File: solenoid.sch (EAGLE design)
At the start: 43 parts, among them U1 QS5K2TR, U2 QS5K2TR, U3 QS5K2TR, U4 QS5K2TR, U5 QS5K2TR, U6 QS5K2TR, Y1 ECS-80-S-4X

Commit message: potentially finished schematic
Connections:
- new net SOLI1_1: U1.TR1_DRAIN
- new net SOLI1_2: U1.TR2_DRAIN
- net GPIO0: now also U2.TR2_GATE
- net GPIO1: now also U2.TR1_GATE
- net GPIO10: now also U4.TR1_GATE
- net GPIO11: now also U4.TR2_GATE
- net GPIO12: now also U5.TR1_GATE
- net GPIO13: now also U5.TR2_GATE
- net GPIO14: now also U6.TR1_GATE
- net GPIO15: now also U6.TR2_GATE
- net GPIO2: now also U1.TR2_GATE
- net GPIO3: now also U1.TR1_GATE
- net GPIO8: now also U3.TR1_GATE
- net GPIO9: now also U3.TR2_GATE
- net SOL2_1: now also U2.TR1_DRAIN
- net SOL2_2: now also U2.TR2_DRAIN
- net SOL3_1: now also U3.TR1_DRAIN
- net SOL3_2: now also U3.TR2_DRAIN
- net SOL4_1: now also U4.TR1_DRAIN
- net SOL4_2: now also U4.TR2_DRAIN
- net SOL5_1: now also U5.TR1_DRAIN
- net SOL5_2: now also U5.TR2_DRAIN
- net SOL6_1: now also U6.TR1_DRAIN
- net SOL6_2: now also U6.TR2_DRAIN
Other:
- note added: "NMOS ARRAY"
- moved on the sheet: U1, U2, U3, U4, U5, U6

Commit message: solenoid work
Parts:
- removed U3, U4, U5, U6: QS5K2TR, QS5K2TR:QS5K2TR
- U1, U2: value QS5K2TR -> ULN2003V12; device QS5K2TR:QS5K2TR -> ULN2003V12:ULN2003V12
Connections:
- removed net SOLI1_1: U1.TR1_DRAIN
- removed net SOLI1_2: U1.TR2_DRAIN
- net 12V: now also U1.COM, U2.COM; no longer U1.TR1_TR2_SOURCE, U2.TR1_TR2_SOURCE, U3.TR1_TR2_SOURCE, U4.TR1_TR2_SOURCE, U5.TR1_TR2_SOURCE, U6.TR1_TR2_SOURCE
- net GND: now also U1.GND, U2.GND
- net GPIO0: now also U1.IN6; no longer U2.TR2_GATE
- net GPIO1: now also U1.IN5; no longer U2.TR1_GATE
- net GPIO10: now also U2.IN3; no longer U4.TR1_GATE
- net GPIO11: now also U2.IN4; no longer U4.TR2_GATE
- net GPIO12: now also U2.IN5; no longer U5.TR1_GATE
- net GPIO13: now also U2.IN6; no longer U5.TR2_GATE
- net GPIO14: now also U1.IN1; no longer U6.TR1_GATE
- net GPIO15: now also U1.IN2; no longer U6.TR2_GATE
- net GPIO2: now also U1.IN4; no longer U1.TR2_GATE
- net GPIO3: now also U1.IN3; no longer U1.TR1_GATE
- net GPIO8: now also U2.IN1; no longer U3.TR1_GATE
- net GPIO9: now also U2.IN2; no longer U3.TR2_GATE
- net SOL1_1: now also U1.OUT3
- net SOL1_2: now also U1.OUT4
- net SOL2_1: now also U1.OUT5; no longer U2.TR1_DRAIN
- net SOL2_2: now also U1.OUT6; no longer U2.TR2_DRAIN
- net SOL3_1: now also U2.OUT1; no longer U3.TR1_DRAIN
- net SOL3_2: now also U2.OUT2; no longer U3.TR2_DRAIN
- net SOL4_1: now also U2.OUT3; no longer U4.TR1_DRAIN
- net SOL4_2: now also U2.OUT4; no longer U4.TR2_DRAIN
- net SOL5_1: now also U2.OUT5; no longer U5.TR1_DRAIN
- net SOL5_2: now also U2.OUT6; no longer U5.TR2_DRAIN
- net SOL6_1: now also U1.OUT1; no longer U6.TR1_DRAIN
- net SOL6_2: now also U1.OUT2; no longer U6.TR2_DRAIN

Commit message: uwu
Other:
- note added: "NPN Array"
- note removed: "NMOS ARRAY"
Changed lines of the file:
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@@
 <text x="342.9" y="55.88" size="1.778" layer="91">Pin 5 (VDDA)</text>
 <text x="370.84" y="-33.02" size="5.08" layer="91">T21 Connector for 12V, CAN, GND</text>
-<text x="10.16" y="-17.78" size="6.4516" layer="91">NMOS ARRAY</text>
+<text x="10.16" y="-17.78" size="6.4516" layer="91">NPN Array</text>
 </plain>
 <instances>

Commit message: k
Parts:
- removed U2: ULN2003V12, ULN2003V12:ULN2003V12
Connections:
- removed net SOL1_2: J1.1, U1.OUT4
- removed net SOL2_2: J2.1, U1.OUT6
- removed net SOL3_2: J5.1, U2.OUT2
- removed net SOL4_2: J6.1, U2.OUT4
- removed net SOL5_2: J7.1, U2.OUT6
- removed net SOL6_2: J8.1, U1.OUT2
- new net GPIO4: U1.IN4
- new net GPIO5: U1.IN5
- new net GPIO6: U1.IN6
- net 12V: now also J1.1, J2.1, J5.1, J6.1, J7.1, J8.1; no longer U2.COM
- net GND: no longer U2.GND
- net GPIO0: no longer U1.IN6
- net GPIO1: now also U1.IN1; no longer U1.IN5
- net GPIO10: no longer U2.IN3
- net GPIO11: no longer U2.IN4
- net GPIO12: no longer U2.IN5
- net GPIO13: no longer U2.IN6
- net GPIO14: no longer U1.IN1
- net GPIO15: no longer U1.IN2
- net GPIO2: now also U1.IN2; no longer U1.IN4
- net GPIO8: no longer U2.IN1
- net GPIO9: no longer U2.IN2
- net SOL1_1: now also U1.OUT1; no longer U1.OUT3
- net SOL2_1: now also U1.OUT2; no longer U1.OUT5
- net SOL3_1: now also U1.OUT3; no longer U2.OUT1
- net SOL4_1: now also U1.OUT4; no longer U2.OUT3
- net SOL5_1: now also U1.OUT5; no longer U2.OUT5
- net SOL6_1: now also U1.OUT6; no longer U1.OUT1

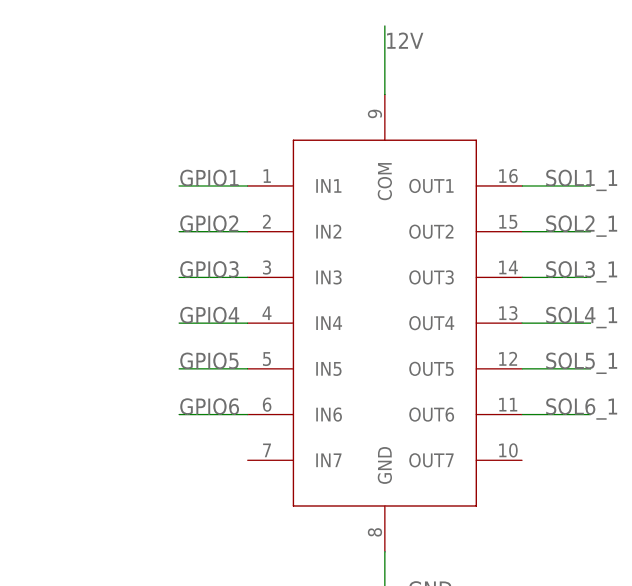
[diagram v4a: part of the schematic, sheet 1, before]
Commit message: next I make solenoid thingies 20 width
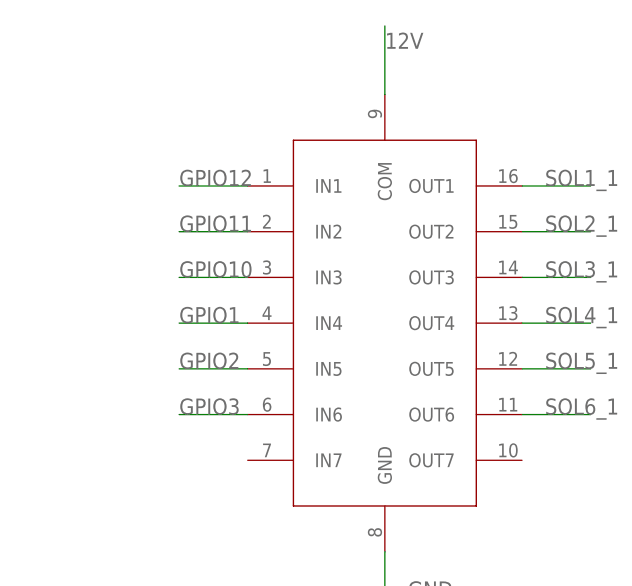
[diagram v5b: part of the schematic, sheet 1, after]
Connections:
- removed net GPIO4: U1.IN4
- removed net GPIO5: U1.IN5
- removed net GPIO6: U1.IN6
- net GPIO1: now also U1.IN4; no longer U1.IN1
- net GPIO10: now also U1.IN3
- net GPIO11: now also U1.IN2
- net GPIO12: now also U1.IN1
- net GPIO2: now also U1.IN5; no longer U1.IN2
- net GPIO3: now also U1.IN6; no longer U1.IN3
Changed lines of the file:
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@@
 </segment>
 <segment>
-<wire x1="15.24" y1="-50.8" x2="7.62" y2="-50.8" width="0.1524" layer="91"/>
-<label x="7.62" y="-50.8" size="1.778" layer="95"/>
-<pinref part="U1" gate="G$1" pin="IN1"/>
+<wire x1="15.24" y1="-66.04" x2="7.62" y2="-66.04" width="0.1524" layer="91"/>
+<label x="7.62" y="-66.04" size="1.778" layer="95"/>
+<pinref part="U1" gate="G$1" pin="IN4"/>
 </segment>
 </net>
@@
 </segment>
 <segment>
-<wire x1="15.24" y1="-60.96" x2="7.62" y2="-60.96" width="0.1524" layer="91"/>
-<label x="7.62" y="-60.96" size="1.778" layer="95"/>
-<pinref part="U1" gate="G$1" pin="IN3"/>
+<wire x1="15.24" y1="-76.2" x2="7.62" y2="-76.2" width="0.1524" layer="91"/>
+<label x="7.62" y="-76.2" size="1.778" layer="95"/>
+<pinref part="U1" gate="G$1" pin="IN6"/>
 </segment>
 </net>
@@
 </segment>
 <segment>
-<wire x1="15.24" y1="-55.88" x2="7.62" y2="-55.88" width="0.1524" layer="91"/>
-<label x="7.62" y="-55.88" size="1.778" layer="95"/>
-<pinref part="U1" gate="G$1" pin="IN2"/>
+<wire x1="15.24" y1="-71.12" x2="7.62" y2="-71.12" width="0.1524" layer="91"/>
+<label x="7.62" y="-71.12" size="1.778" layer="95"/>
+<pinref part="U1" gate="G$1" pin="IN5"/>
 </segment>
 </net>
@@
 <label x="350.52" y="99.06" size="1.778" layer="95" rot="R90"/>
 </segment>
+<segment>
+<wire x1="15.24" y1="-60.96" x2="7.62" y2="-60.96" width="0.1524" layer="91"/>
+<label x="7.62" y="-60.96" size="1.778" layer="95"/>
+<pinref part="U1" gate="G$1" pin="IN3"/>
+</segment>
 </net>
 <net name="GPIO9" class="0">
@@
 <label x="353.06" y="99.06" size="1.778" layer="95" rot="R90"/>
 </segment>
+<segment>
+<wire x1="15.24" y1="-55.88" x2="7.62" y2="-55.88" width="0.1524" layer="91"/>
+<label x="7.62" y="-55.88" size="1.778" layer="95"/>
+<pinref part="U1" gate="G$1" pin="IN2"/>
+</segment>
 </net>
 <net name="GPIO12" class="0">
@@
 <label x="358.14" y="99.06" size="1.778" layer="95" rot="R90"/>
 </segment>
+<segment>
+<wire x1="15.24" y1="-50.8" x2="7.62" y2="-50.8" width="0.1524" layer="91"/>
+<label x="7.62" y="-50.8" size="1.778" layer="95"/>
+<pinref part="U1" gate="G$1" pin="IN1"/>
+</segment>
 </net>
 <net name="SOL3_1" class="0">
@@
 </segment>
 </net>
-<net name="GPIO4" class="0">
-<segment>
-<wire x1="15.24" y1="-66.04" x2="7.62" y2="-66.04" width="0.1524" layer="91"/>
-<label x="7.62" y="-66.04" size="1.778" layer="95"/>
-<pinref part="U1" gate="G$1" pin="IN4"/>
-</segment>
-</net>
-<net name="GPIO5" class="0">
-<segment>
-<wire x1="15.24" y1="-71.12" x2="7.62" y2="-71.12" width="0.1524" layer="91"/>
-<label x="7.62" y="-71.12" size="1.778" layer="95"/>
-<pinref part="U1" gate="G$1" pin="IN5"/>
-</segment>
-</net>
-<net name="GPIO6" class="0">
-<segment>
-<wire x1="15.24" y1="-76.2" x2="7.62" y2="-76.2" width="0.1524" layer="91"/>
-<label x="7.62" y="-76.2" size="1.778" layer="95"/>
-<pinref part="U1" gate="G$1" pin="IN6"/>
-</segment>
-</net>

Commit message: new connectors. another hole. v2
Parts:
- removed C3, C4: 100nF, SparkFun-Capacitors:4.7UF0603
- removed C5: 0.01uF, SparkFun-Capacitors:4.7UF0603
- removed J4, J5, J6, J7, J8: (no value), SparkFun-Connectors:CONN_02
- removed RESET: SWITCH, DiscreteComponents:SWITCH
- added H2, H3: 6-32-HOLE, Mounting Holes:6-32-HOLE
- added U$1: DISCRETECOMPONENTS_SWITCH, Push button - FSM2JMTR:DISCRETECOMPONENTS_SWITCH
- J1, J2, J3: device SparkFun-Connectors:CONN_02 -> Phoenix Contact PTSM-04-V-1778573:PXC-PTSM-04-V-1778573
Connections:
- removed net GPIO0: U$3.PB7
- removed net GPIO13: U$3.PA8
- removed net GPIO14: U$3.PA9
- removed net GPIO15: U$3.PA10
- removed net GPIO8: U$3.PA3
- removed net GPIO9: U$3.PA4
- net +3V3: no longer C3.1, C4.1, C5.1
- net 12V: now also J1.4, J2.4, J3.4; no longer J1.1, J2.1, J3.2, J5.1, J6.1, J7.1, J8.1
- net CAN_H: now also J3.3; no longer J4.2
- net CAN_L: now also J3.2; no longer J4.1
- net GND: now also U$1.P$1; no longer C3.2, C4.2, C5.2, RESET.P$1
- net NRST: now also U$1.P$2; no longer RESET.P$2
- net SOL1_1: now also J1.3; no longer J1.2
- net SOL2_1: now also J1.2; no longer J2.2
- net SOL3_1: now also J1.1; no longer J5.2
- net SOL4_1: now also J2.3; no longer J6.2
- net SOL5_1: now also J2.2; no longer J7.2
- net SOL6_1: now also J2.1; no longer J8.2
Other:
- note removed: "T21 Connector for 12V, CAN, GND"

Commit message: final touch-ups
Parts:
- removed C18: 47uF, SparkFun-Capacitors:47UF-POLAR-PANASONIC_D-35V-20%
- added C3: 47UF-POLAR-PANASONIC_D-50V-20%, Panasonic 47 uF cap - EEE-1CA470SP:47UF-POLAR-PANASONIC_D-50V-20%
- C7: value 4.7uF -> 0.1uF
- C8, C9: value 4.7uF -> 20pF
- R1, R3: value 1k -> 0
- R2: value 1k -> 10k
- R7: value (none) -> 470
- U$8: device PI_Shield_Library:TCAN337D -> STM and CAN parts:TCAN337D
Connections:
- net 12V: now also C3.+; no longer C18.+
- net GND: now also C3.-; no longer C18.-
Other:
- note removed: "Power Indication LEDs"
- moved on the sheet: C1, C10, C11, C2, C6, C7, C8, C9, D1, D2, D4, H2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
